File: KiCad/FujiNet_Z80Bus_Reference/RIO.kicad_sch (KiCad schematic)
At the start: 17 parts, among them IC19 7432N, IC2 7404N, IC20 7408N, IC4 7432N, IC5 7408N

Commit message: Massive fix to KiCad Labels
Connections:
- net Z80_HARDLOCK_SET is gone; now on net Z80_HARDLOCK_RESET: RIO_DECODER1.11 (B8)
- net VCC: no longer R11.2, R9.2, RIO1.32 (VCC)
- net ESP_CONTROL_BUSRQ renamed ESP_CONTROL.BUSRQ
- net ESP_CONTROL_IORQ renamed ESP_CONTROL.IORQ
- net ESP_CONTROL_MEMRQ renamed ESP_CONTROL.MEMRQ
- net ESP_CONTROL_ROMCS renamed ESP_CONTROL.ROMCS
- net ROM_WR_PROTECT renamed ESP_ROM_WR_PROTECT
- net Z80_MEMRQ renamed Z80_CONTROL.MEMRQ
- net Z80_RD renamed Z80_CONTROL.RD
- net Z80_WR renamed Z80_CONTROL.WR
- new net +5V: R11.2, R9.2, RIO1.32 (VCC)
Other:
- moved on the sheet: R9

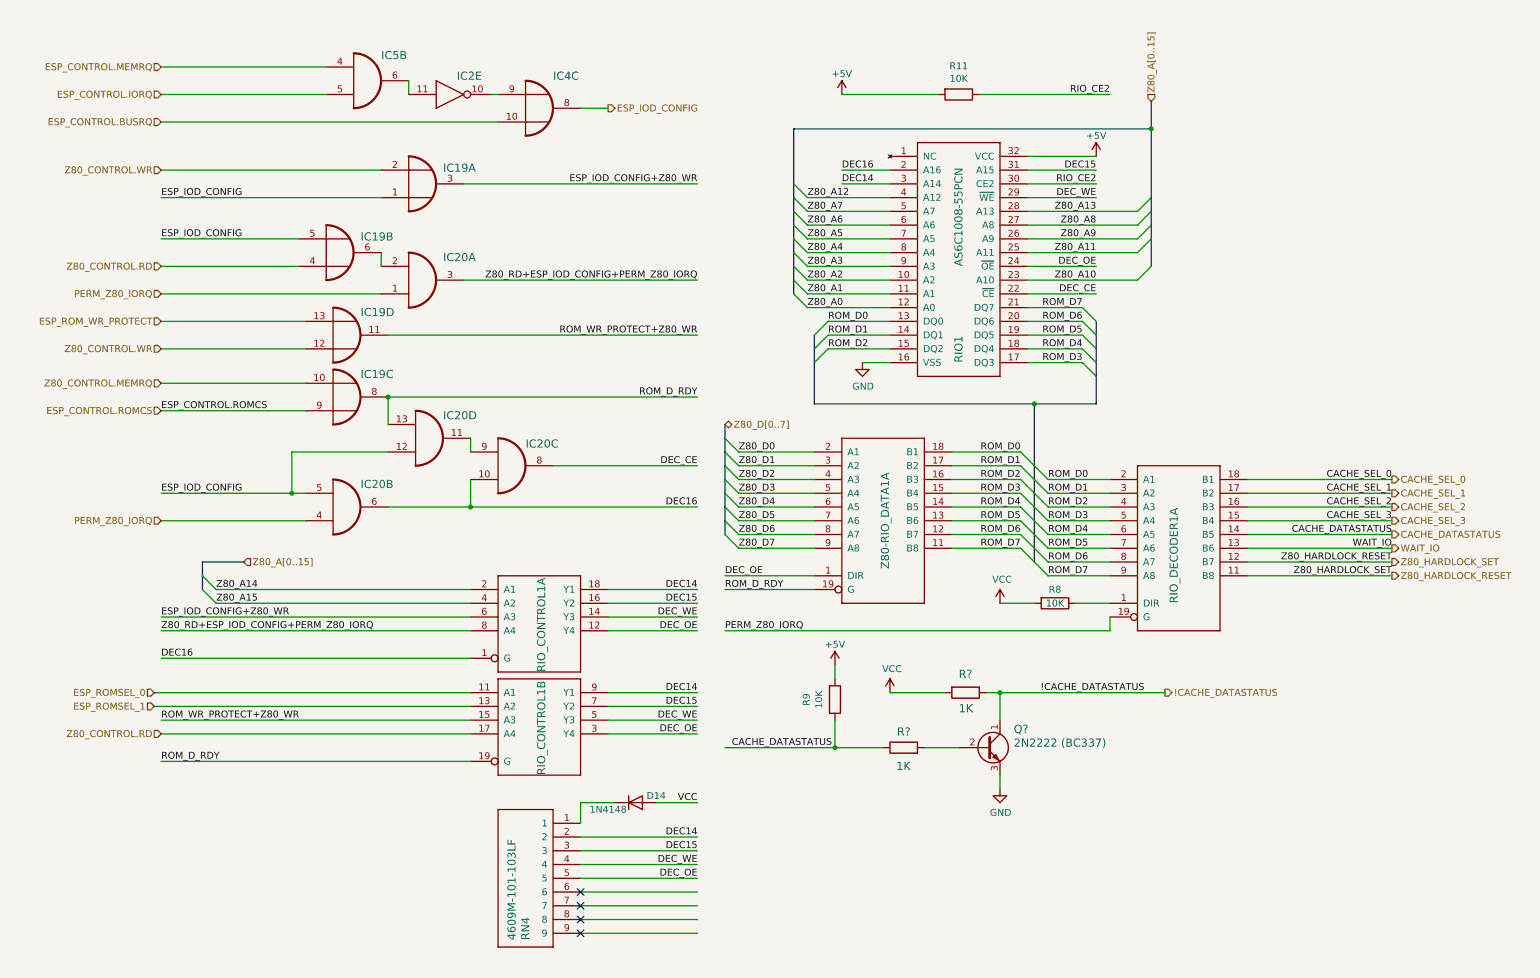
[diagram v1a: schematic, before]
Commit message: KiCad Labels mostly fixed
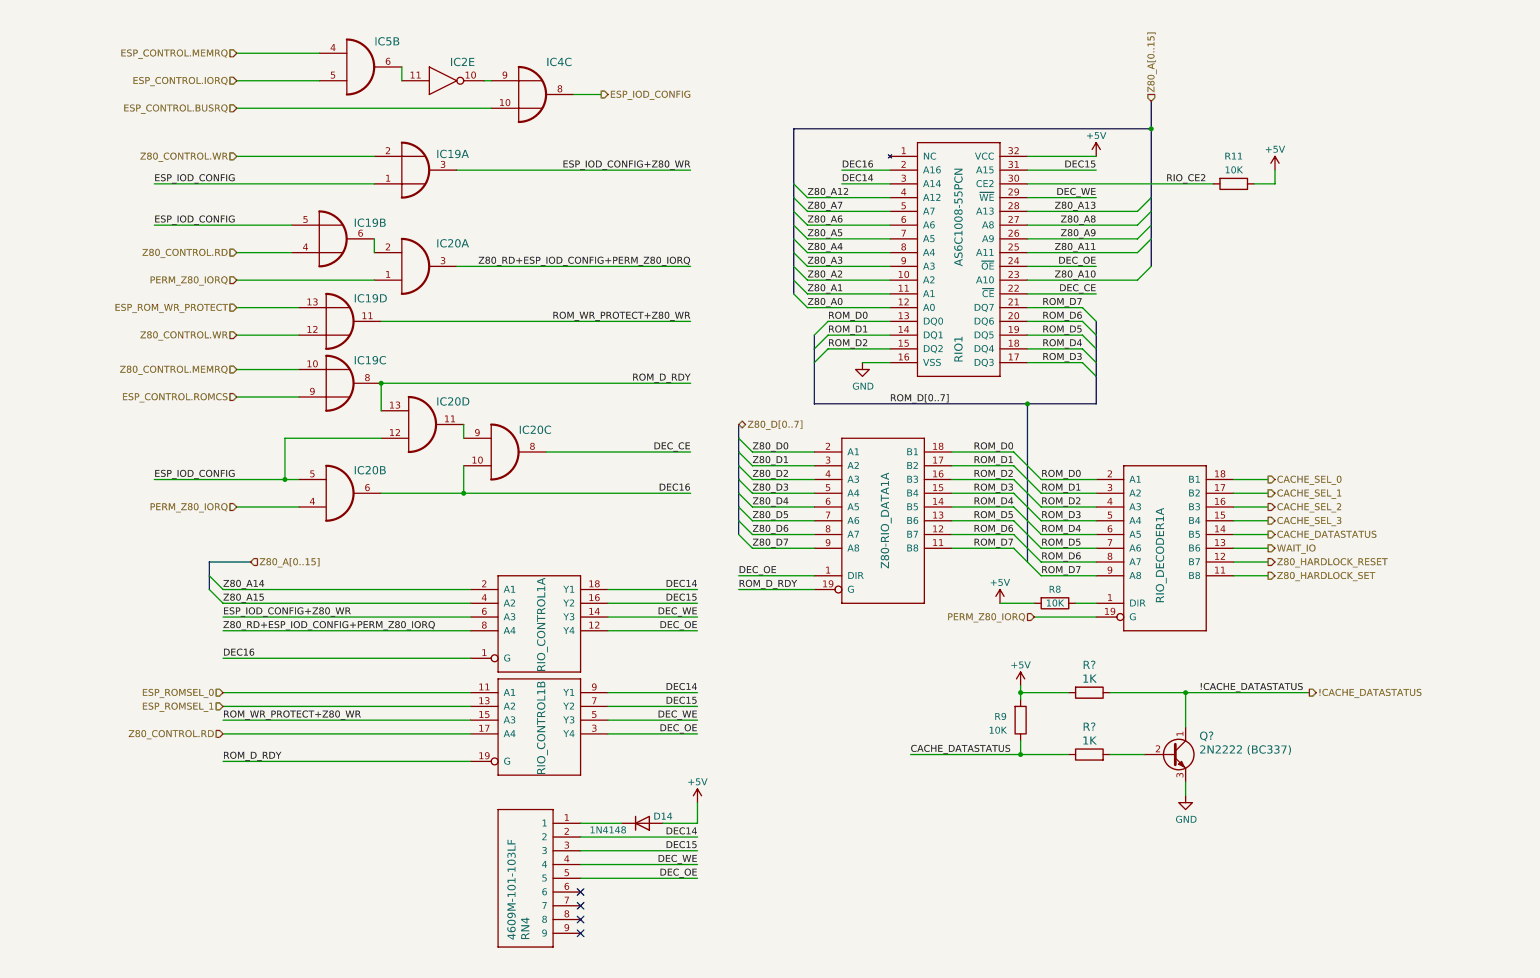
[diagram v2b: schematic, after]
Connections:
- net VCC is gone; now on net +5V: D14.2 (A), R8.2, R?.2
- net +5V: now also R11.1; no longer R11.2
- net RIO_CE2: now also R11.2; no longer R11.1
- net Z80_HARDLOCK_RESET: no longer RIO_DECODER1.11 (B8)
- new net Z80_HARDLOCK_SET: RIO_DECODER1.11 (B8)
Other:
- moved on the sheet: D14, IC19A, IC19B, IC19C, IC19D, IC20A, IC20B, IC20C, IC20D, IC2E, IC4C, IC5B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
